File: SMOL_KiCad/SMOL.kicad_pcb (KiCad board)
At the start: 2 copper layers, 12.7 x 14.2 mm, 13 parts, among them Q1 Q_NMOS_GSD, U1 TLV61220, U2 ATTINY13-20SSU

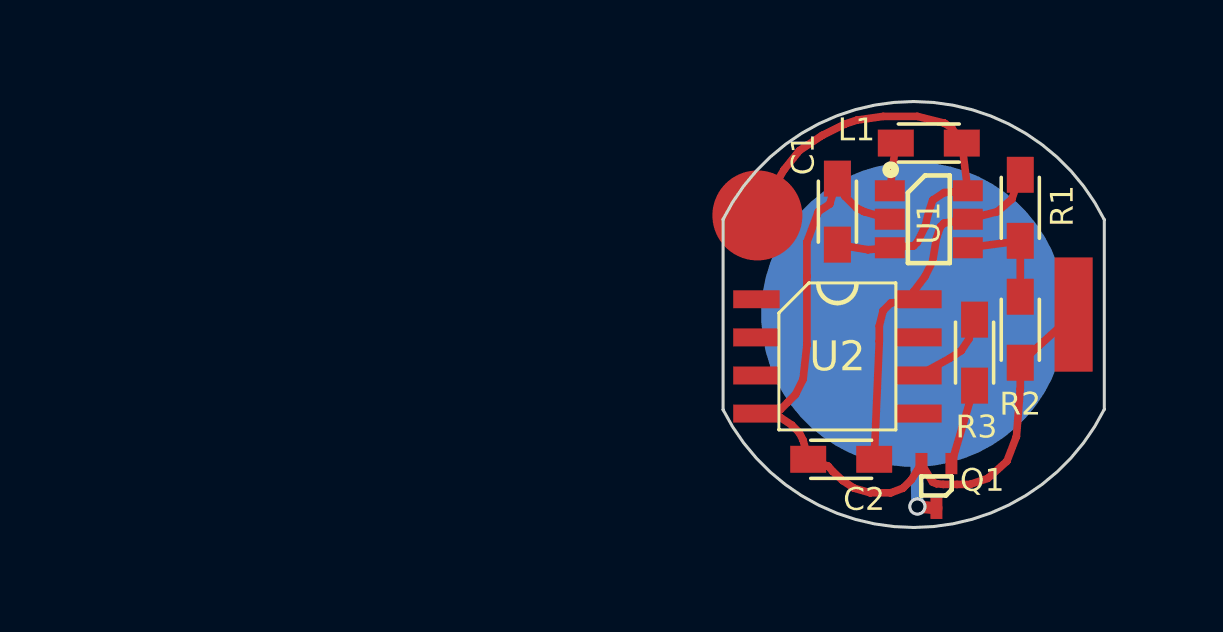
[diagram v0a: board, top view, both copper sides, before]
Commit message: Rearranged components, set up for ATTiny10 instead of 13
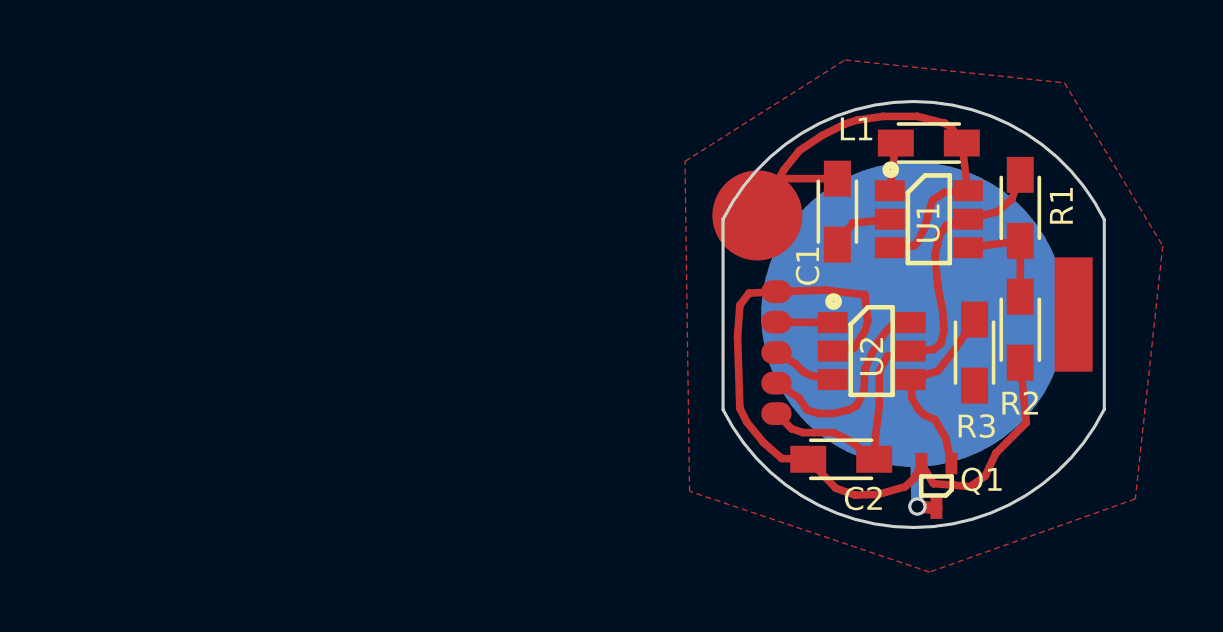
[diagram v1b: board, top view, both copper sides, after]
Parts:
- added REF**: TPI_pad, SMOL_footprints:TPI_pad, F.Cu at (97.0, 100.8)
- added REF**: TPI_pad, SMOL_footprints:TPI_pad, F.Cu at (97.0, 101.9)
- added REF**: TPI_pad, SMOL_footprints:TPI_pad, F.Cu at (97.0, 102.9)
- added REF**: TPI_pad, SMOL_footprints:TPI_pad, F.Cu at (97.0, 103.9)
- added REF**: TPI_pad, SMOL_footprints:TPI_pad, F.Cu at (97.0, 104.9)
- C1, C2: value 10μ -> 10μF
- L1: value 4.7μ -> 4.7μH
- R1: value 1M -> 1MΩ
- R2: value 180k -> 180kΩ
- R3: value 1k -> 20kΩ
- U2: value ATTINY13-20SSU -> ATTINY10-TS; footprint SMOL_footprints:SOIC-8_3.9x4.9mm_Pitch1.27mm -> SMOL_footprints:SuperSOT-6
- moved U2 1.16 mm to (100.2, 102.8)
- turned C1 to 270 degrees
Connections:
- R3 pad 1: Net-(Q1-Pad1) -> /Anode
- R3 pad 2: Net-(R3-Pad2) -> Net-(Q1-Pad1)
- U2 pad 2: Net-(U2-Pad2) -> /Anode
- U2 pad 4: /Anode -> Net-(Q1-Pad1)
- U2 pad 5: Net-(U2-Pad5) -> /μC_Vcc
- U2 pad 6: Net-(R3-Pad2) -> Net-(U2-Pad6)
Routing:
- net Net-(U2-Pad6): track 0.00 -> 6.74 mm
- net /μC_Vcc: track 12.4 -> 16.5 mm
- net Net-(Q1-Pad1): track 2.71 -> 6.35 mm
- net Net-(R3-Pad2): track 2.79 -> 0.00 mm
- net Net-(U2-Pad3): track 0.00 -> 2.13 mm
- net Net-(U2-Pad1): track 0.00 -> 1.88 mm
- net /Cathode: track 15.7 -> 17.5 mm
- net /Anode: track 27.8 -> 27.2 mm
- added copper zone on F.Cu, net /Anode
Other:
- net class Thick added: clearance 0.3048, trace_width 0.8128, via_dia 0.6096, via_drill 0.4064

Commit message: Added diode and re-wired output from U2
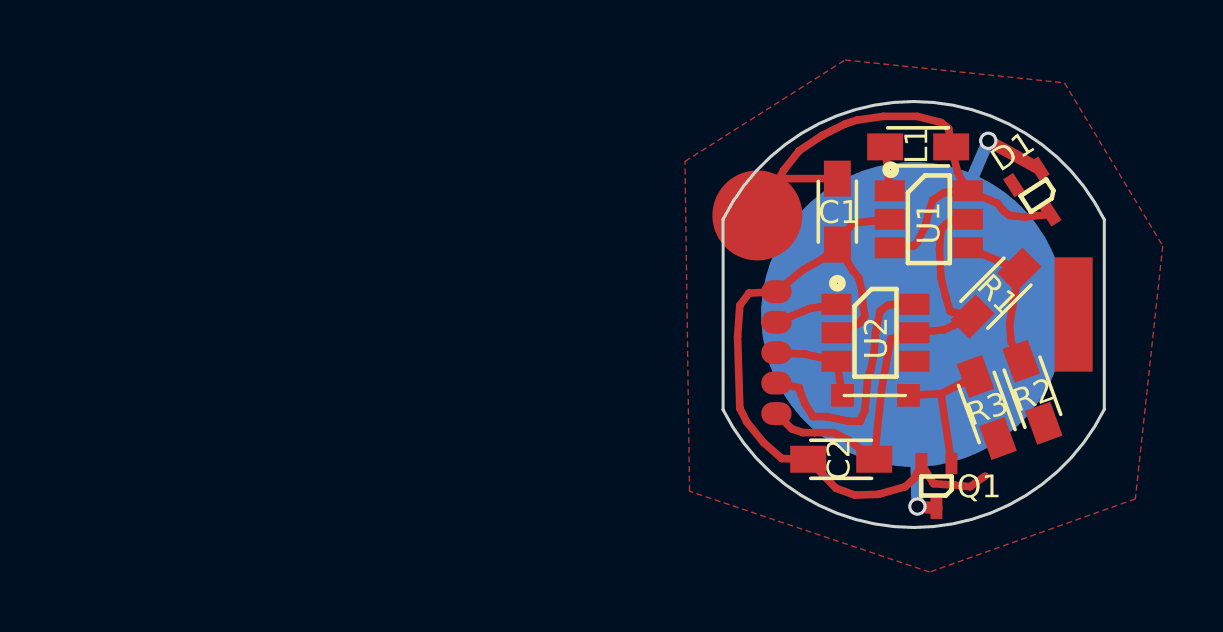
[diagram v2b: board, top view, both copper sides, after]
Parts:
- added D1: D_SOT523, SMOL_footprints:SOT523_HandSoldering, F.Cu at (105.8, 97.6)
- added J1: Bridge, SMOL_footprints:0603_Jumper, F.Cu at (100.3, 104.3)
- moved R1 2.96 mm to (104.3, 100.9), turned to 45 degrees
- moved R2 2.12 mm to (105.6, 104.2), turned to 290 degrees
- moved R3 1.87 mm to (104.0, 104.7), turned to 110 degrees
- moved U2 0.62 mm to (100.3, 102.2)
- moved L1 0.38 mm to (101.8, 96.0)
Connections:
- Q1 pad 1: Net-(Q1-Pad1) -> Net-(J1-Pad1)
- R3 pad 2: Net-(Q1-Pad1) -> Net-(J1-Pad1)
- U2 pad 3: Net-(U2-Pad3) -> Net-(J1-Pad2)
- U2 pad 4: Net-(Q1-Pad1) -> Net-(U2-Pad4)
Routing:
- net /Spring_Contact: track 7.04 -> 15.3 mm, vias 1 -> 2
- net Net-(Q1-Pad1): track 6.35 -> 0.00 mm
- net Net-(J1-Pad1): track 0.00 -> 4.72 mm
- net /Anode: track 27.2 -> 23.7 mm
- net /Cathode: track 17.5 -> 20.4 mm
- net Net-(J1-Pad2): track 0.00 -> 2.21 mm
- net Net-(U2-Pad6): track 6.74 -> 8.41 mm
- net Net-(R1-Pad2): track 3.63 -> 5.02 mm
- net /μC_Vcc: track 16.5 -> 15.2 mm
- net Net-(U2-Pad3): track 2.13 -> 0.97 mm

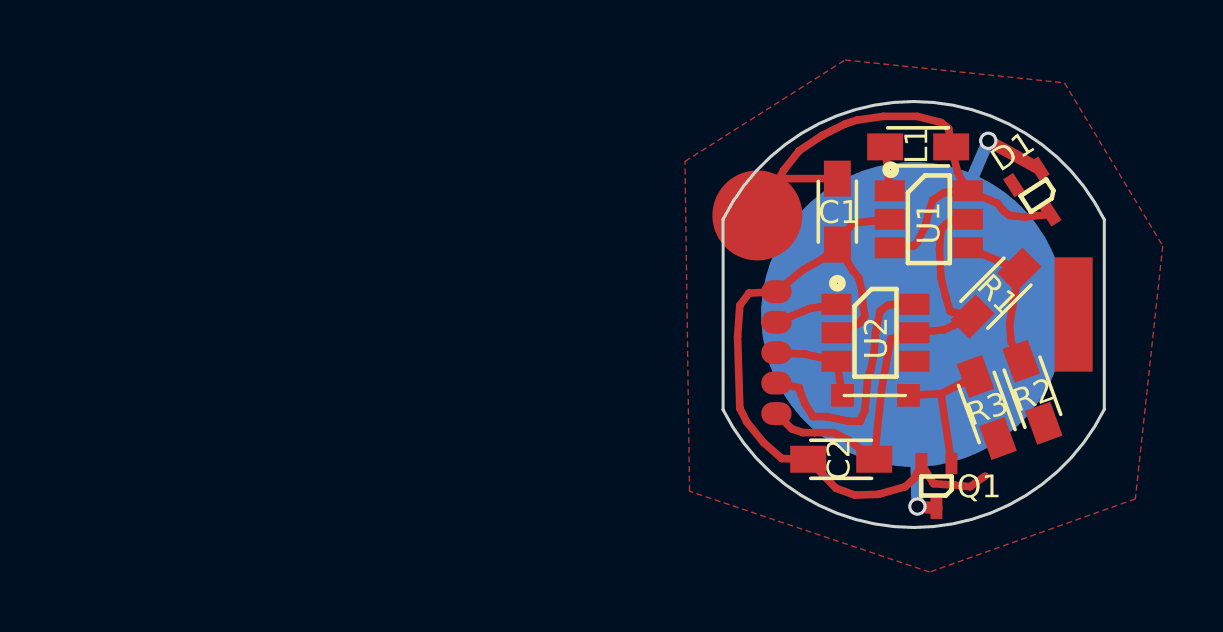
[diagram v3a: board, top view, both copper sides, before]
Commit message: Revision 5: added an FFC connector for easier programming (at the expense of my commitment to hand-solderability)
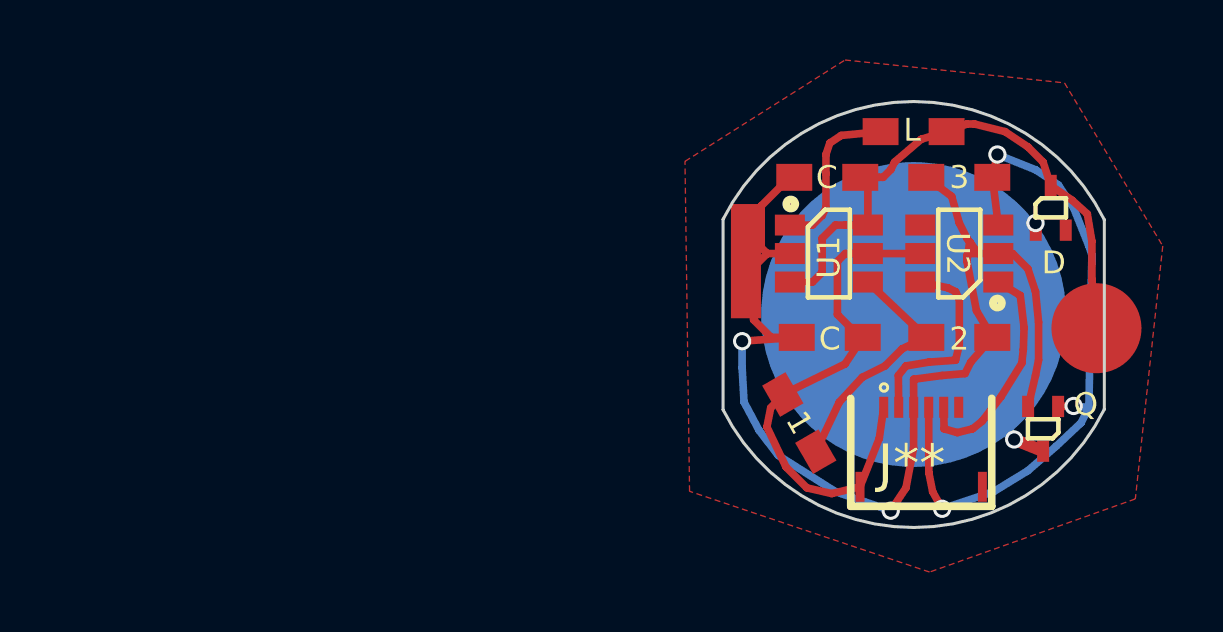
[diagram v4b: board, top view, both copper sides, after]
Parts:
- removed C1, C2: 10μF, SMOL_footprints:0603_HandSoldering
- removed D1: D_SOT523, SMOL_footprints:SOT523_HandSoldering
- removed J1: Bridge, SMOL_footprints:0603_Jumper
- removed L1: 4.7μH, SMOL_footprints:0603_HandSoldering
- removed R1: 1MΩ, SMOL_footprints:0603_HandSoldering
- removed R2: 180kΩ, SMOL_footprints:0603_HandSoldering
- removed R3: 20kΩ, SMOL_footprints:0603_HandSoldering
- removed REF** (x5): TPI_pad, SMOL_footprints:TPI_pad
- added 1: 1MΩ, SMOL_footprints:0603_HandSoldering, F.Cu at (97.8, 105.2)
- added 2: 180kΩ, SMOL_footprints:0603_HandSoldering, F.Cu at (103.1, 102.4)
- added 3: 20kΩ, SMOL_footprints:0603_HandSoldering, F.Cu at (103.1, 97.0)
- added C: 10μF, SMOL_footprints:0603_HandSoldering, F.Cu at (98.7, 97.0)
- added C: 10μF, SMOL_footprints:0603_HandSoldering, F.Cu at (98.8, 102.4)
- added D: D_SOT523, SMOL_footprints:SOT523_HandSoldering, F.Cu at (106.2, 98.0)
- added J**: FFC6-0.5mm, SMOL_footprints:FFC6-0.5mm, F.Cu at (101.9, 104.4)
- added L: 4.7μH, SMOL_footprints:0603_HandSoldering, F.Cu at (101.6, 95.5)
- moved TP1 11.9 mm to (107.7, 102.1)
- moved TP2 11.1 mm to (96.0, 99.8)
- moved Q 4.03 mm to (105.9, 105.4)
- moved U2 3.85 mm to (103.1, 99.6), turned to 180 degrees
- moved U1 3.52 mm to (98.8, 99.6)
- moved G*** 0.22 mm to (101.8, 101.4), turned to 270 degrees
- renumbered Q1 to Q
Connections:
- Q pad 1: Net-(J1-Pad1) -> Net-(Q1-Pad1)
- U2 pad 3: Net-(J1-Pad2) -> Net-(Q1-Pad1)
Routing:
- net Net-(Q1-Pad1): track 0.00 -> 23.0 mm, vias 0 -> 3
- net /Anode: track 23.7 -> 39.8 mm, vias 0 -> 2
- net Net-(U2-Pad1): track 2.10 -> 7.58 mm
- net Net-(J1-Pad1): track 4.72 -> 0.00 mm
- net Net-(L1-Pad2): track 1.47 -> 5.45 mm
- net /Spring_Contact: track 15.3 -> 11.7 mm
- net Net-(R1-Pad2): track 5.02 -> 8.22 mm
- net /μC_Vcc: track 15.2 -> 17.9 mm
- net Net-(J1-Pad2): track 2.21 -> 0.00 mm
- net Net-(U2-Pad6): track 8.41 -> 6.69 mm
- net /Cathode: track 20.4 -> 19.1 mm
- net Net-(U2-Pad3): track 0.97 -> 0.00 mm

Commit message: Revision 6 - a card-edge connector with a plug-in programmer
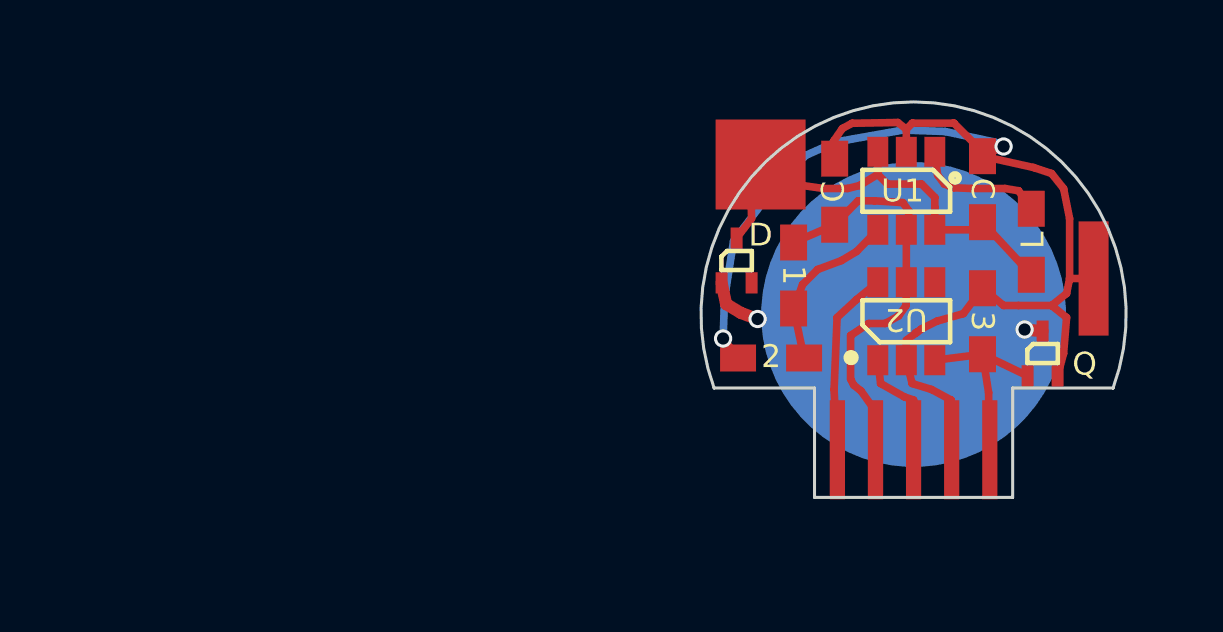
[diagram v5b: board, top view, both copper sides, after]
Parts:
- removed J**: FFC6-0.5mm, SMOL_footprints:FFC6-0.5mm
- added J1: Conn_01x05, SMOL_footprints:edgeconn, F.Cu at (99.1, 106.5)
- moved TP1 12.5 mm to (96.5, 96.6)
- moved TP2 11.6 mm to (107.6, 100.4)
- moved D 10.6 mm to (95.7, 99.8)
- moved 2 6.31 mm to (96.8, 103.0), turned to 180 degrees
- moved L 5.37 mm to (105.5, 99.2), turned to 90 degrees
- moved C 5.19 mm to (103.9, 97.4), turned to 90 degrees
- moved 1 4.92 mm to (97.6, 100.3), turned to 270 degrees
- moved C 4.86 mm to (99.0, 97.5), turned to 90 degrees
- moved 3 4.86 mm to (103.9, 101.8), turned to 270 degrees
- moved U1 3.32 mm to (101.4, 97.5), turned to 270 degrees
- moved U2 2.87 mm to (101.4, 101.8), turned to 90 degrees
- moved Q 2.51 mm to (105.9, 102.9), turned to 0 degrees
- moved G*** 0.23 mm to (101.7, 101.7), turned to 90 degrees
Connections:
- U2 pad 4: Net-(U2-Pad4) -> (no net)
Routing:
- net Net-(Q1-Pad1): track 23.0 -> 6.85 mm, vias 3 -> 0
- net /Anode: track 39.8 -> 44.0 mm
- net /Cathode: track 19.1 -> 15.3 mm
- net /μC_Vcc: track 17.9 -> 14.6 mm
- net Net-(R1-Pad2): track 8.22 -> 5.74 mm
- net Net-(U2-Pad1): track 7.58 -> 5.56 mm
- net Net-(L1-Pad2): track 5.45 -> 4.40 mm
- removed copper zone on F.Cu, net /Anode
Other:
- board size 12.7 x 14.2 mm -> 14.2 x 13.2 mm
- rule pad_to_mask_clearance: 0.1524 -> 0.0508

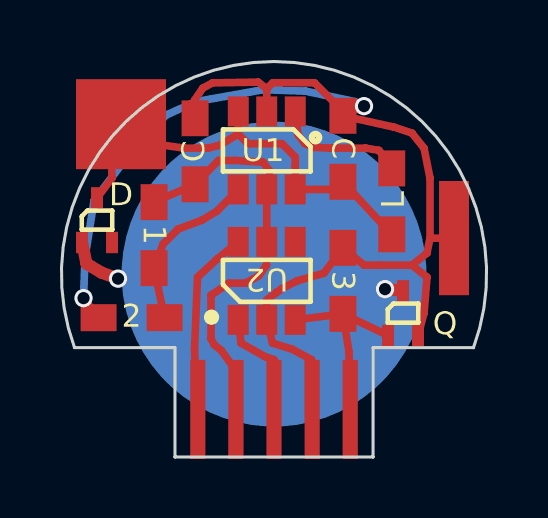
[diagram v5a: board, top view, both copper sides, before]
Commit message: Tweaked the bottom silkscreen and moved vias to make it legible
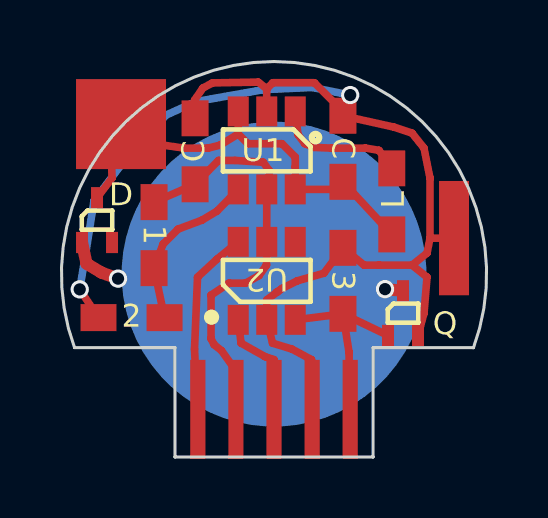
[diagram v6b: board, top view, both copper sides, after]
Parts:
- removed the G*** at (101.7, 101.7)
- added G***: credits2-title, SMOL_footprints:credits2-title, B.Cu at (101.6, 101.7)
- added G***: credits2-name, SMOL_footprints:credits2-name, B.Cu at (101.6, 101.7)
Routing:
- net /Anode: track 44.0 -> 43.5 mm

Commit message: Updated gerbs, added folder for AVR programs
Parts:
- added REF***: OSHW-Symbol_6.7x6mm_SilkScreen, Symbols:OSHW-Symbol_6.7x6mm_SilkScreen, F.Cu at (92.5, 107.1)
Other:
- outline, holes or cut-outs redrawn

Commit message: Working toward new release, updating images and documents
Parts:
- moved REF*** 17.0 mm to (76.5, 101.3)
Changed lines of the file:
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@@
-(kicad_pcb (version 20171130) (host pcbnew "(5.0.1)-3")
+(kicad_pcb (version 20171130) (host pcbnew "(5.0.2)-1")
   (general
     (thickness 0.508)
@@
       (rotate (xyz 0 0 0))
     )
+    (model ${KISYS3DMOD}/Package_TO_SOT_SMD.3dshapes/SuperSOT-6.wrl
+      (at (xyz 0 0 0))
+      (scale (xyz 1 1 1))
+      (rotate (xyz 0 0 0))
+    )
   )
   (module SMOL_footprints:SuperSOT-6 (layer F.Cu)
@@
     (pad 1 smd rect (at -1.3 -0.95 90) (size 1 0.7) (layers F.Cu F.Mask)
       (net 7 "Net-(U2-Pad1)"))
-    (model ${KISYS3DMOD}/TO_SOT_Packages_SMD.3dshapes/SuperSOT-6.wrl
+    (model ${KISYS3DMOD}/Package_TO_SOT_SMD.3dshapes/SuperSOT-6.wrl
       (at (xyz 0 0 0))
       (scale (xyz 1 1 1))
@@
     (pad 2 smd rect (at 1.1 0 270) (size 1.2 0.9) (layers F.Cu F.Mask)
       (net 9 "Net-(Q1-Pad1)"))
-    (model ${KISYS3DMOD}/Resistors_SMD.3dshapes/R_0603.wrl
+    (model ${KISYS3DMOD}/Resistor_SMD.3dshapes/R_0603_1608Metric.wrl
       (at (xyz 0 0 0))
       (scale (xyz 1 1 1))
@@
     (pad 2 smd rect (at 1.1 0 90) (size 1.2 0.9) (layers F.Cu F.Mask)
       (net 4 "Net-(L1-Pad2)"))
-    (model ${KISYS3DMOD}/Resistors_SMD.3dshapes/R_0603.wrl
+    (model ${KISYS3DMOD}/Inductor_SMD.3dshapes/L_0603_1608Metric.wrl
       (at (xyz 0 0 0))
       (scale (xyz 1 1 1))
@@
     (pad 2 smd rect (at 1.1 0 90) (size 1.2 0.9) (layers F.Cu F.Mask)
       (net 2 /Anode))
-    (model ${KISYS3DMOD}/Resistors_SMD.3dshapes/R_0603.wrl
+    (model ${KISYS3DMOD}/Capacitor_SMD.3dshapes/C_0603_1608Metric.wrl
       (at (xyz 0 0 0))
       (scale (xyz 1 1 1))
@@
     (pad 1 smd rect (at -1.1 0 180) (size 1.2 0.9) (layers F.Cu F.Mask)
       (net 6 "Net-(R1-Pad2)"))
-    (model ${KISYS3DMOD}/Resistors_SMD.3dshapes/R_0603.wrl
+    (model ${KISYS3DMOD}/Resistor_SMD.3dshapes/R_0603_1608Metric.wrl
       (at (xyz 0 0 0))
       (scale (xyz 1 1 1))
@@
     (pad 2 smd rect (at 1.1 0 90) (size 1.2 0.9) (layers F.Cu F.Mask)
       (net 2 /Anode))
-    (model ${KISYS3DMOD}/Resistors_SMD.3dshapes/R_0603.wrl
+    (model ${KISYS3DMOD}/Capacitor_SMD.3dshapes/C_0603_1608Metric.wrl
       (at (xyz 0 0 0))
       (scale (xyz 1 1 1))
@@
     (pad 2 smd rect (at 1.099999 0 270) (size 1.2 0.9) (layers F.Cu F.Mask)
       (net 6 "Net-(R1-Pad2)"))
-    (model ${KISYS3DMOD}/Resistors_SMD.3dshapes/R_0603.wrl
+    (model ${KISYS3DMOD}/Resistor_SMD.3dshapes/R_0603_1608Metric.wrl
       (at (xyz 0 0 0))
       (scale (xyz 1 1 1))
@@
     (pad 1 smd rect (at -0.5 0.745) (size 0.4 0.71) (layers F.Cu F.Mask)
       (net 9 "Net-(Q1-Pad1)"))
-    (model TO_SOT_Packages_SMD.3dshapes/SOT-23.wrl
-      (at (xyz 0 0 0))
-      (scale (xyz 0.5 0.5 0.5))
+    (model ${KISYS3DMOD}/Package_TO_SOT_SMD.3dshapes/SOT-323_SC-70.wrl
+      (at (xyz 0 0 0))
+      (scale (xyz 0.7 0.7 0.6))
       (rotate (xyz 0 0 -90))
     )
@@
     (pad 3 smd rect (at 0 -0.745) (size 0.4 0.71) (layers F.Cu F.Mask)
       (net 1 /Cathode))
-    (model TO_SOT_Packages_SMD.3dshapes/SOT-23.wrl
-      (at (xyz 0 0 0))
-      (scale (xyz 0.5 0.5 0.5))
+    (model ${KISYS3DMOD}/Package_TO_SOT_SMD.3dshapes/SOT-323_SC-70.wrl
+      (at (xyz 0 0 0))
+      (scale (xyz 0.7 0.7 0.6))
       (rotate (xyz 0 0 -90))
     )
@@
   )
   (module Symbols:OSHW-Symbol_6.7x6mm_SilkScreen (layer F.Cu)
-    (at 92.456 107.061)
+    (at 76.454 101.346)
     (descr "Open Source Hardware Symbol")
     (tags "Logo Symbol OSHW")
